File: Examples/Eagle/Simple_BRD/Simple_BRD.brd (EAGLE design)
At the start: 61 x 52.1 mm, 8 parts

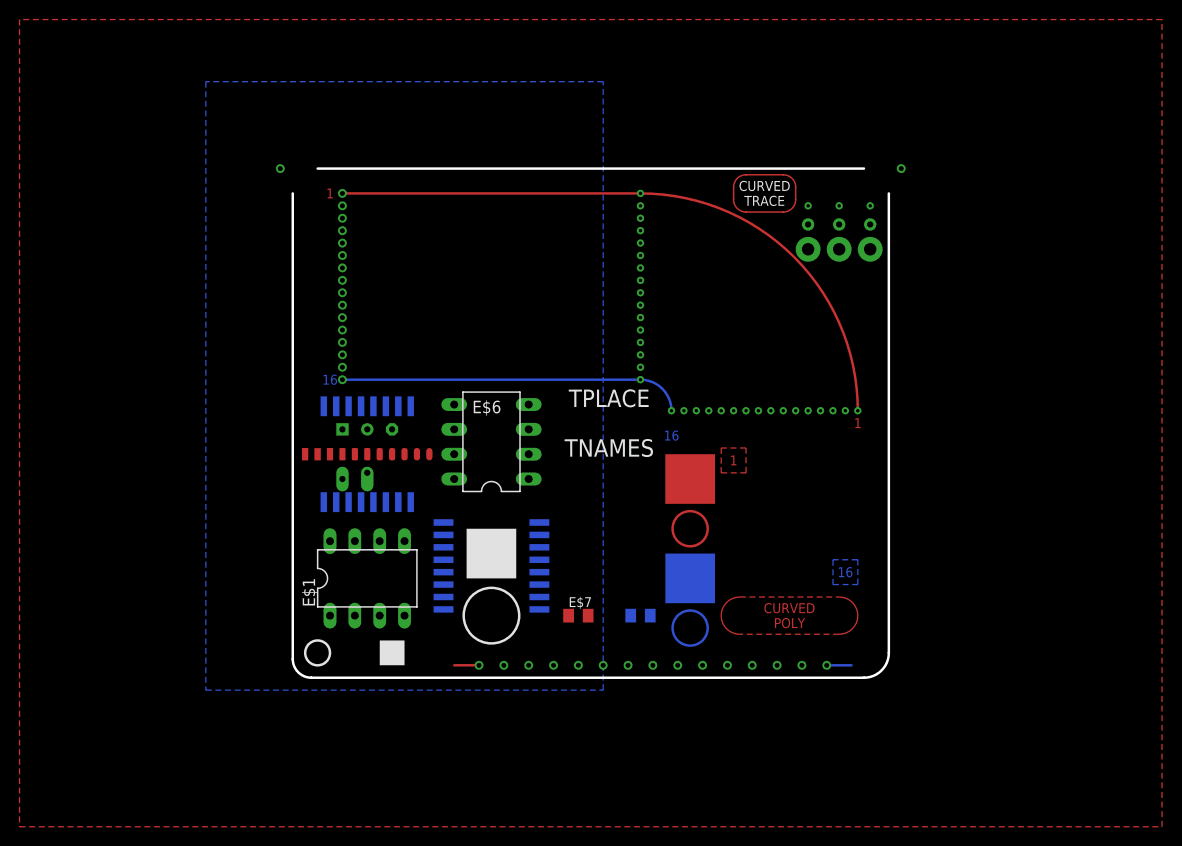
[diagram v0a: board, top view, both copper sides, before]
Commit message: Updated all example json files
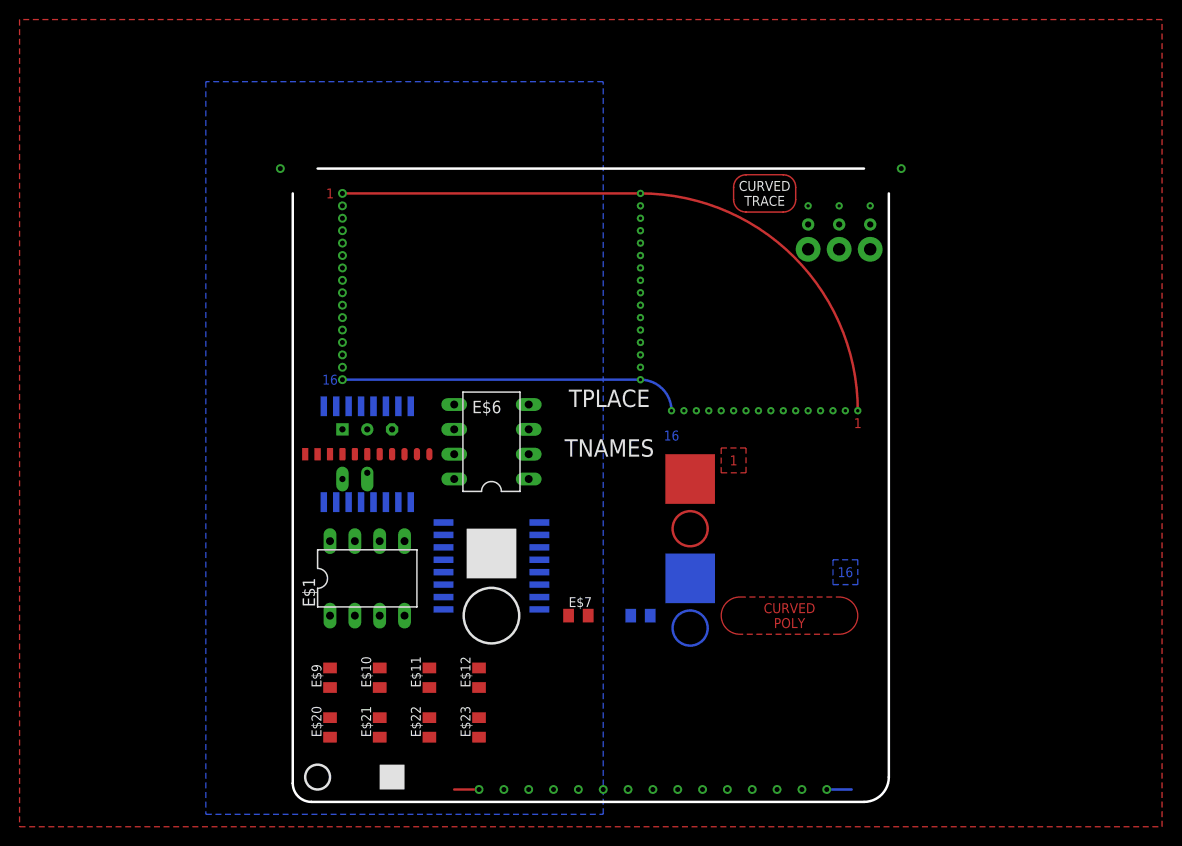
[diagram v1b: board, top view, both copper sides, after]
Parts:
- added E$10, E$11, E$12, E$20, E$21, E$22, E$23, E$9: 10uF, adafruit:C0805K
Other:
- board size 61 x 52.1 mm -> 61 x 64.8 mm
